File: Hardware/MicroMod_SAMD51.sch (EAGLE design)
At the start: 30 parts, among them J2 MICROMOD-2222, U1 W25QXX128MBIT-6X5-NO_CENTER, U2 ATSAMD51J20A-A, Y1 32.768kHz

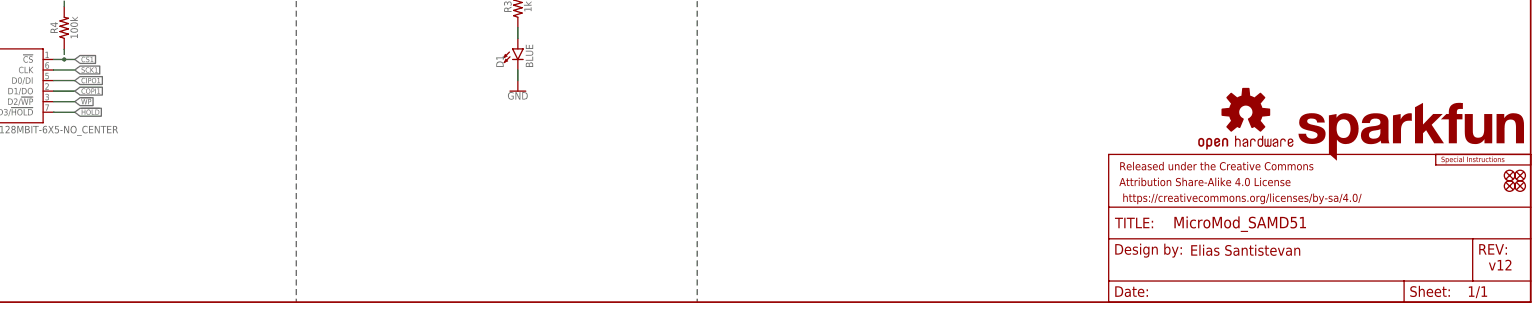
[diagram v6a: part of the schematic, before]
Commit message: Fixes swapped nets COPI/CIPO at flash chip
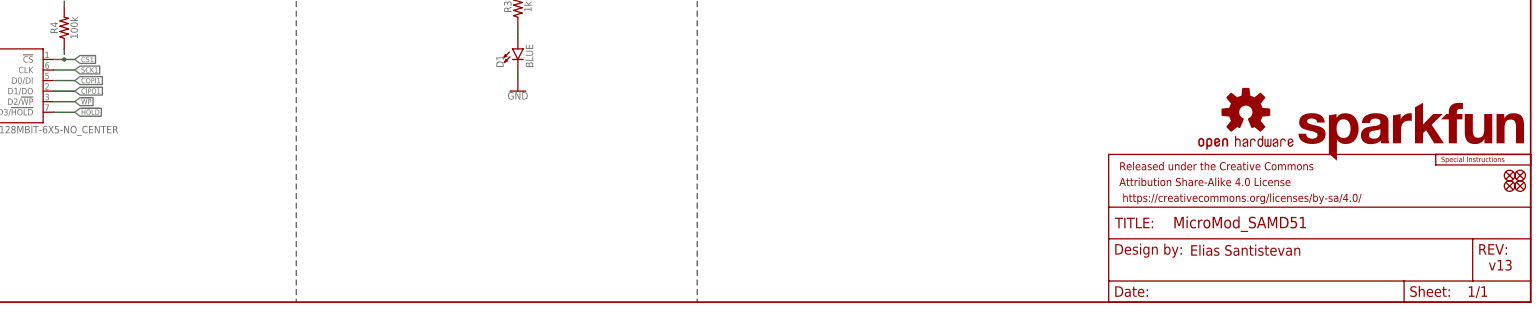
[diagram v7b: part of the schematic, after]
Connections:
- net CIPO1: now also U1.D1/DO; no longer U1.D0/DI
- net COPI1: now also U1.D0/DI; no longer U1.D1/DO
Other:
- note added: "v13"
- note removed: "v12"
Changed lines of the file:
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@@
 <?xml version="1.0" encoding="utf-8"?>
 <!DOCTYPE eagle SYSTEM "eagle.dtd">
-<eagle version="9.5.2">
+<eagle version="9.6.2">
 <drawing>
 <settings>
@@
 <sheet>
 <plain>
-<text x="421.64" y="7.62" size="2.54" layer="94" font="vector">v12</text>
+<text x="421.64" y="7.62" size="2.54" layer="94" font="vector">v13</text>
 <text x="250.64" y="273.78" size="2.54" layer="94" font="vector" align="center">M.2 Connector</text>
 <wire x1="231.14" y1="279.4" x2="231.14" y2="111.76" width="0.1524" layer="97" style="longdash"/>
@@
 <net name="COPI1" class="0">
 <segment>
+<wire x1="88.9" y1="210.82" x2="86.36" y2="210.82" width="0.1524" layer="91"/>
+<label x="86.36" y="210.82" size="1.27" layer="95" rot="R180" xref="yes"/>
+<pinref part="U2" gate="G$1" pin="PA09(SER0_1,SER2_0,ADC)"/>
+</segment>
+<segment>
+<pinref part="U1" gate="U1" pin="D0/DI"/>
+<wire x1="76.2" y1="53.34" x2="81.28" y2="53.34" width="0.1524" layer="91"/>
+<label x="81.28" y="53.34" size="1.27" layer="95" xref="yes"/>
+</segment>
+</net>
+<net name="CIPO1" class="0">
+<segment>
+<wire x1="88.9" y1="208.28" x2="86.36" y2="208.28" width="0.1524" layer="91"/>
+<label x="86.36" y="208.28" size="1.27" layer="95" rot="R180" xref="yes"/>
+<pinref part="U2" gate="G$1" pin="PA10(SER0_2,SER2_2,ADC)"/>
+</segment>
+<segment>
 <pinref part="U1" gate="U1" pin="D1/DO"/>
 <wire x1="76.2" y1="50.8" x2="81.28" y2="50.8" width="0.1524" layer="91"/>
 <label x="81.28" y="50.8" size="1.27" layer="95" xref="yes"/>
 </segment>
-<segment>
-<wire x1="88.9" y1="210.82" x2="86.36" y2="210.82" width="0.1524" layer="91"/>
-<label x="86.36" y="210.82" size="1.27" layer="95" rot="R180" xref="yes"/>
-<pinref part="U2" gate="G$1" pin="PA09(SER0_1,SER2_0,ADC)"/>
-</segment>
-</net>
-<net name="CIPO1" class="0">
-<segment>
-<wire x1="88.9" y1="208.28" x2="86.36" y2="208.28" width="0.1524" layer="91"/>
-<label x="86.36" y="208.28" size="1.27" layer="95" rot="R180" xref="yes"/>
-<pinref part="U2" gate="G$1" pin="PA10(SER0_2,SER2_2,ADC)"/>
-</segment>
-<segment>
-<pinref part="U1" gate="U1" pin="D0/DI"/>
-<wire x1="76.2" y1="53.34" x2="81.28" y2="53.34" width="0.1524" layer="91"/>
-<label x="81.28" y="53.34" size="1.27" layer="95" xref="yes"/>
-</segment>
-</net>
+</net>

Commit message: Updates to latest parts
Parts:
- L1: device SparkFun-Coils:FERRITE_BEAD-0402-30OHM-100MHZ -> SparkFun-Coils:FERRITE_BEAD-0402-30Ω-100MHZ
